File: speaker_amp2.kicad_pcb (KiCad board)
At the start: 2 copper layers, 72 parts, among them J1 Molex_430450227, J2 Molex_430450227, J3 Molex_430450227, J4 Molex_430450227, J5 Molex_1053101106, U1 TAS5822MDCPR, U2 TAS5822MDCPR

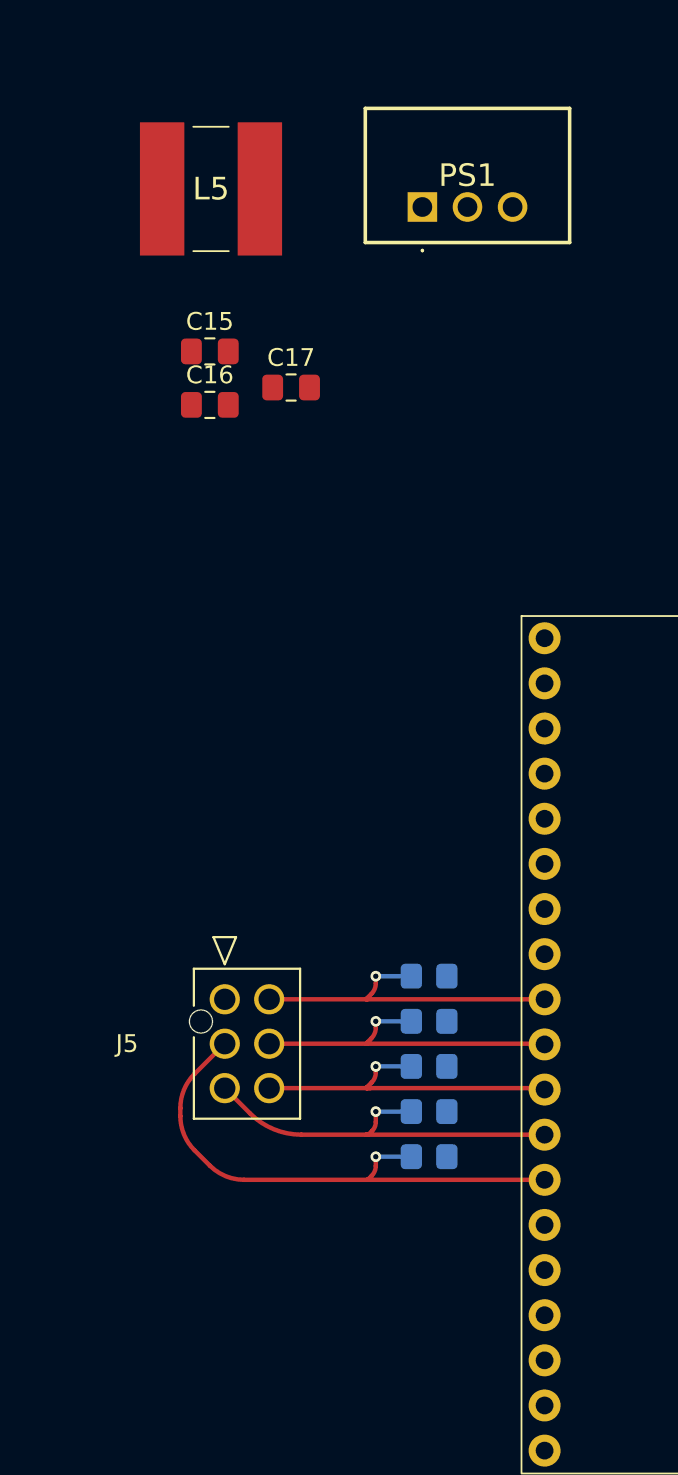
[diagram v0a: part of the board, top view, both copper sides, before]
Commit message: placed 3.3V to pcb
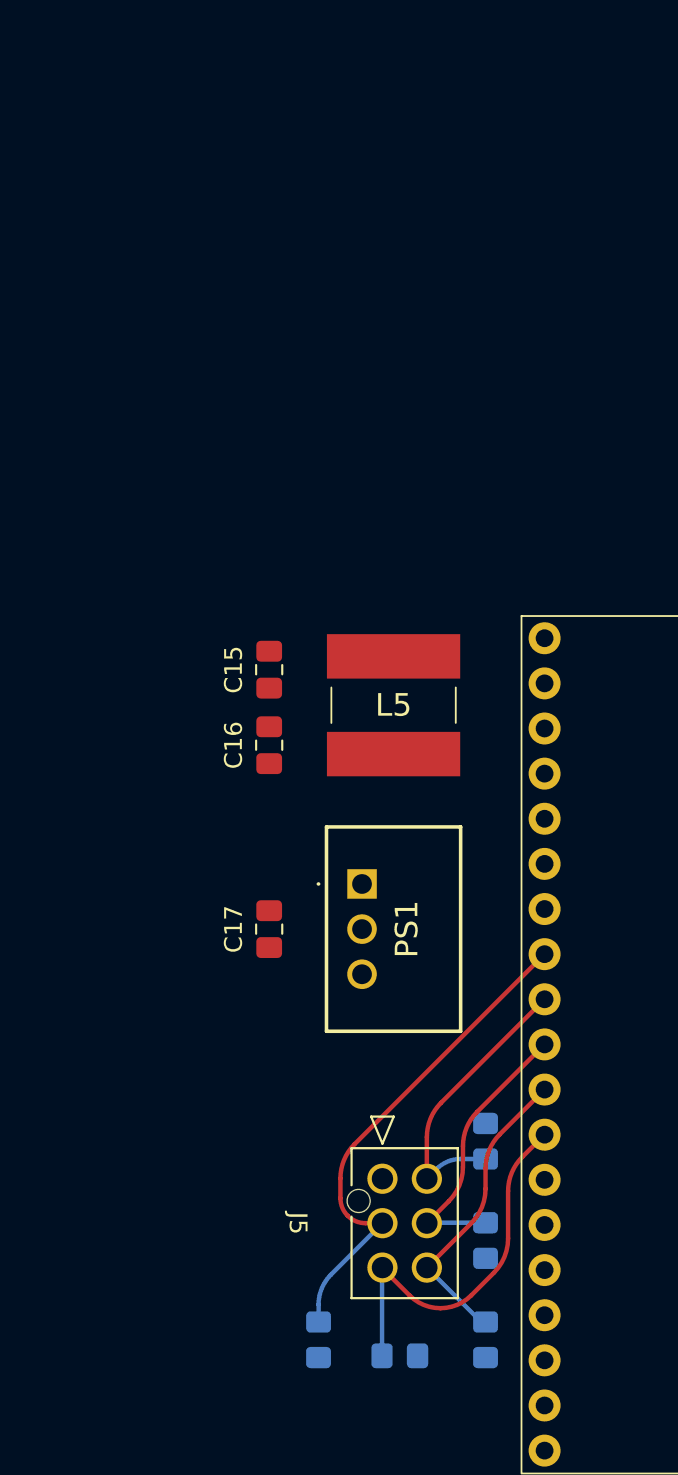
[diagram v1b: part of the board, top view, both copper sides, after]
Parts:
- moved PS1 38.3 mm to (36.0, 99.1), turned to -90 degrees
- moved L5 30.8 mm to (37.8, 89.0), turned to -90 degrees
- moved C17 30.5 mm to (30.8, 101.6), turned to 90 degrees
- moved C16 19.4 mm to (30.8, 91.2), turned to -90 degrees
- moved C15 18.2 mm to (30.8, 87.0), turned to 90 degrees
- moved R15 15.7 mm to (42.9, 124.7), turned to -90 degrees
- moved R12 13.8 mm to (38.1, 125.6)
- moved J5 13.4 mm to (37.1, 115.7)
- moved R14 12.7 mm to (42.9, 119.1), turned to -90 degrees
- moved R11 12.0 mm to (33.5, 124.7), turned to -90 degrees
- moved R13 9.82 mm to (42.9, 113.5), turned to 90 degrees
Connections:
- MCU1 pad 13: /Previous -> unconnected-(MCU1-GPIO12-Pad13)
- MCU1 pad 8: unconnected-(MCU1-GPIO33-Pad8) -> /Previous
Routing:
- net /Volume+: track 19.0 -> 15.9 mm, vias 1 -> 0
- net /Volume-: track 19.2 -> 16.4 mm, vias 1 -> 0
- net /Previous: track 30.8 -> 28.5 mm, vias 1 -> 0
- net /Play/Pause: track 19.1 -> 17.1 mm, vias 1 -> 0
- net /Next: track 22.5 -> 21.5 mm, vias 1 -> 0

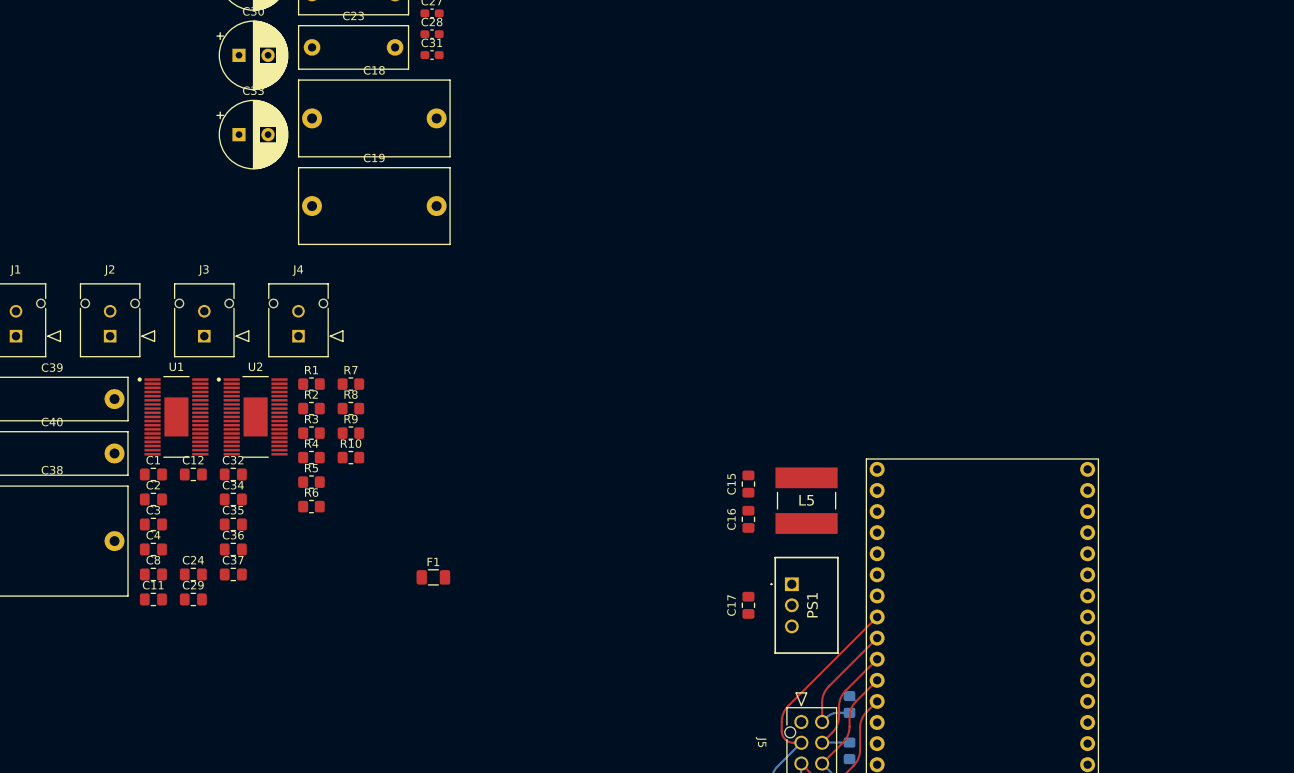
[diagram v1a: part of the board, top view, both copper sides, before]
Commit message: changed amplifiers in schematic to match PCB pins
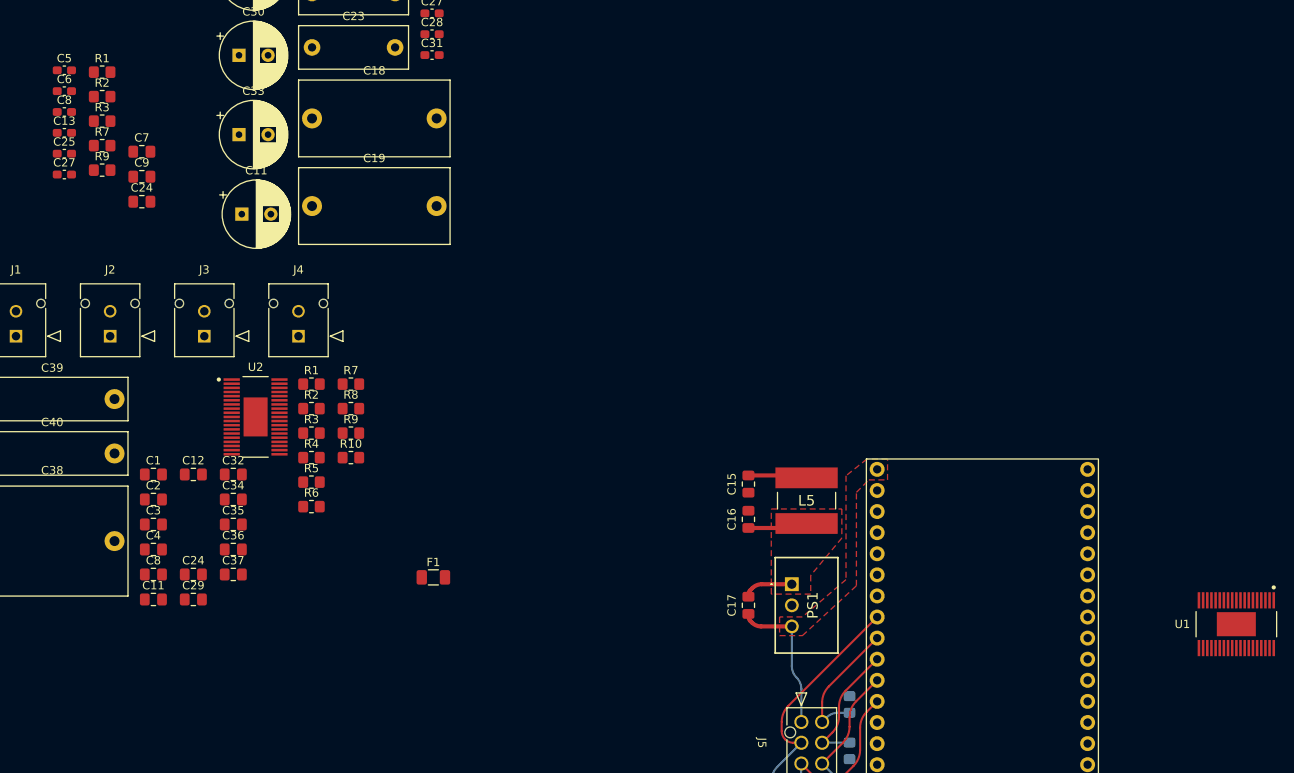
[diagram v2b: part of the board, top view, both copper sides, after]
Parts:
- added C11: 390u, Capacitor_THT:CP_Radial_D8.0mm_P3.50mm, F.Cu at (-30.2, 54.5)
- added C13: 1u, Capacitor_SMD:C_0603_1608Metric_Pad1.08x0.95mm_HandSolder, F.Cu at (-51.6, 44.7)
- added C24: 4.7u, Capacitor_SMD:C_0805_2012Metric_Pad1.18x1.45mm_HandSolder, F.Cu at (-42.3, 53.0)
- added C25: 0.1u, Capacitor_SMD:C_0603_1608Metric_Pad1.08x0.95mm_HandSolder, F.Cu at (-51.6, 47.2)
- added C27: 1u, Capacitor_SMD:C_0603_1608Metric_Pad1.08x0.95mm_HandSolder, F.Cu at (-51.6, 49.7)
- added C5: 0.1u, Capacitor_SMD:C_0603_1608Metric_Pad1.08x0.95mm_HandSolder, F.Cu at (-51.6, 37.2)
- added C6: 1u, Capacitor_SMD:C_0603_1608Metric_Pad1.08x0.95mm_HandSolder, F.Cu at (-51.6, 39.7)
- added C7: 4.7u, Capacitor_SMD:C_0805_2012Metric_Pad1.18x1.45mm_HandSolder, F.Cu at (-42.3, 47.0)
- added C8: 0.1u, Capacitor_SMD:C_0603_1608Metric_Pad1.08x0.95mm_HandSolder, F.Cu at (-51.6, 42.2)
- added C9: 22u, Capacitor_SMD:C_0805_2012Metric_Pad1.18x1.45mm_HandSolder, F.Cu at (-42.3, 50.0)
- added R1: 2.2k, Resistor_SMD:R_0805_2012Metric_Pad1.20x1.40mm_HandSolder, F.Cu at (-47.1, 37.4)
- added R2: 2.2k, Resistor_SMD:R_0805_2012Metric_Pad1.20x1.40mm_HandSolder, F.Cu at (-47.1, 40.4)
- added R3: 4.7k, Resistor_SMD:R_0805_2012Metric_Pad1.20x1.40mm_HandSolder, F.Cu at (-47.1, 43.3)
- added R7: 4.7k, Resistor_SMD:R_0805_2012Metric_Pad1.20x1.40mm_HandSolder, F.Cu at (-47.1, 46.2)
- added R9: 4.7k, Resistor_SMD:R_0805_2012Metric_Pad1.20x1.40mm_HandSolder, F.Cu at (-47.1, 49.2)
- moved U1 130.0 mm to (89.5, 103.9), turned to -90 degrees
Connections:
- net Net-(MCU1-GPIO17) renamed /PDN2
- net Net-(U1-SDOUT) renamed /SDOUT1
- C26 pad 1: Net-(U2-AVDD) -> GND
- C26 pad 2: GND -> Net-(U2-AVDD)
- C3 pad 1: Net-(U1-BST_B+) -> Net-(U1-BST_B-)
- C3 pad 2: Net-(U1-OUT_B+) -> Net-(U1-OUT_B-)
- C34 pad 1: Net-(U2-BST_A-) -> Net-(U2-OUT_A+)
- C34 pad 2: Net-(U2-OUT_A+) -> Net-(U2-BST_A-)
- C35 pad 1: Net-(U2-BST_A+) -> Net-(U2-OUT_A+)
- C35 pad 2: Net-(U2-OUT_A+) -> Net-(U2-BST_A+)
- C4 pad 1: Net-(U1-BST_B-) -> Net-(U1-BST_B+)
- C4 pad 2: Net-(U1-OUT_B-) -> Net-(U1-OUT_B+)
- L3 pad 1: Net-(U1-OUT_B+) -> Net-(U1-OUT_B-)
- L4 pad 2: Net-(U1-OUT_B-) -> Net-(U1-OUT_B+)
- L6 pad 1: Net-(U2-OUT_B+) -> Net-(U2-OUT_A+)
- L7 pad 2: Net-(U2-OUT_A+) -> Net-(U2-OUT_B+)
- MCU1 pad 21: Net-(MCU1-GPIO23) -> /ADR1
- MCU1 pad 22: Net-(MCU1-GPIO22) -> /LRCLK
- MCU1 pad 23: Net-(MCU1-GPIO1) -> /SCLK
- MCU1 pad 24: Net-(MCU1-GPIO3) -> /SDIN
- MCU1 pad 25: unconnected-(MCU1-GPIO21-Pad25) -> /SDA
- MCU1 pad 27: Net-(MCU1-GPIO19) -> /SCL
- MCU1 pad 28: Net-(MCU1-GPIO18) -> /PDN1
- MCU1 pad 29: Net-(MCU1-GPIO5) -> /ADR2
- MCU1 pad 31: Net-(MCU1-GPIO16) -> unconnected-(MCU1-GPIO16-Pad31)
- R4 pad 2: Net-(MCU1-GPIO5) -> /SDIN
- R6 pad 1: Net-(MCU1-GPIO16) -> /ADR2
- U1 pad 10: Net-(MCU1-GPIO1) -> /ADR1
- U1 pad 13: Net-(MCU1-GPIO19) -> /LRCLK
- U1 pad 14: Net-(MCU1-GPIO18) -> /SCLK
- U1 pad 15: Net-(MCU1-GPIO5) -> /SDIN
- U1 pad 27: Net-(MCU1-GPIO23) -> /SDA
- U1 pad 28: Net-(MCU1-GPIO22) -> /SCL
- U1 pad 29: Net-(MCU1-GPIO3) -> /PDN1
- U2 pad 10: Net-(MCU1-GPIO16) -> /ADR2
- U2 pad 13: Net-(MCU1-GPIO19) -> /LRCLK
- U2 pad 14: Net-(MCU1-GPIO18) -> /SCLK
- U2 pad 27: Net-(MCU1-GPIO23) -> /SDA
- U2 pad 28: Net-(MCU1-GPIO22) -> /SCL
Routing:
- net +3.3V: track 0.00 -> 17.9 mm
- net Net-(PS1-+VIN): track 0.00 -> 13.3 mm
- net PVDD: track 0.00 -> 7.12 mm
- added copper zone on F.Cu, net +3.3V
- added copper zone on F.Cu, net Net-(PS1-+VIN)

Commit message: placed amp ics, did low-voltage connections
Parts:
- removed the C27 at (-7.34, 30.3)
- U1, U2: footprint Speaker Amp Lib:DCP0038A-IPC_A -> Speaker Amp Lib:DCP0038A-IPC_B
- moved C11 190.2 mm to (141.2, 155.8)
- moved C13 190.2 mm to (151.5, 71.2)
- moved C2 190.2 mm to (141.2, 143.7)
- moved C25 190.2 mm to (130.5, 102.1)
- moved C29 190.2 mm to (146.0, 155.8)
- moved C3 190.2 mm to (141.2, 146.8)
- moved C30 190.2 mm to (151.5, 90.3)
- moved C33 190.2 mm to (151.5, 99.8)
- moved C34 190.2 mm to (150.8, 143.7)
- moved C35 190.2 mm to (150.8, 146.8)
- moved C37 190.2 mm to (150.8, 152.8)
- moved C5 190.2 mm to (130.5, 92.1)
- moved C8 190.2 mm to (141.2, 152.8)
- moved J1 190.2 mm to (124.6, 124.1)
- moved J2 190.2 mm to (136.0, 124.1)
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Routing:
- net PVDD: track 7.12 -> 67.3 mm, vias 0 -> 2
- net +3.3V: track 17.9 -> 60.3 mm, vias 0 -> 2
- net /SDA: track 0.00 -> 42.1 mm, vias 0 -> 2
- net /SCL: track 0.00 -> 36.4 mm, vias 0 -> 2
- net Net-(U2-SDIN): track 0.00 -> 12.6 mm
- net /SDOUT1: track 0.00 -> 6.19 mm
- net /PDN1: track 0.00 -> 5.77 mm, vias 0 -> 1
- net Net-(U2-VR_DIG): track 0.00 -> 3.81 mm
- net Net-(U2-AVDD): track 0.00 -> 3.34 mm
- net Net-(U1-AVDD): track 0.00 -> 3.12 mm
- net Net-(U1-VR_DIG): track 0.00 -> 2.96 mm
- net /SCLK: track 0.00 -> 2.67 mm, vias 0 -> 1
- net /ADR2: track 0.00 -> 2.17 mm, vias 0 -> 1
- net /LRCLK: track 0.00 -> 1.67 mm, vias 0 -> 1
- added copper zone on F.Cu, net Net-(F1-Pad2)

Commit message: changed some components (coils) for smaller ones
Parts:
- removed the C11 at (141.2, 155.8)
- removed the C13 at (82.5, 111.1)
- removed the C13 at (151.5, 71.2)
- removed the C24 at (84.2, 117.8)
- removed the C24 at (139.8, 107.9)
- removed the C25 at (84.0, 120.1)
- removed the C25 at (130.5, 102.1)
- removed the C5 at (174.7, 67.6)
- removed the C6 at (174.7, 70.2)
- removed the C7 at (174.7, 72.7)
- removed the C8 at (141.2, 152.8)
- removed the C8 at (84.5, 98.3)
- removed the C9 at (174.7, 75.2)
- removed the R1 at (160.2, 129.8)
- removed the R2 at (160.2, 132.8)
- removed the R3 at (160.2, 135.8)
- removed the R7 at (165.0, 129.8)
- removed the R9 at (165.0, 135.8)
- added C13: 1u, Capacitor_SMD:C_0603_1608Metric_Pad1.08x0.95mm_HandSolder, F.Cu at (79.2, 96.2)
- added C24: 4.7u, Capacitor_SMD:C_0805_2012Metric_Pad1.18x1.45mm_HandSolder, F.Cu at (77.8, 117.8)
- added C25: 0.1u, Capacitor_SMD:C_0603_1608Metric_Pad1.08x0.95mm_HandSolder, F.Cu at (80.0, 118.0)
- added C8: 0.1u, Capacitor_SMD:C_0603_1608Metric_Pad1.08x0.95mm_HandSolder, F.Cu at (79.8, 83.7)
- added F2: 2A, Fuse:Fuse_1206_3216Metric, F.Cu at (79.8, 138.5)
- added J6: Molex_430450227, Speaker Amp Lib:430450227_MOLEX, F.Cu at (65.3, 138.5)
- C11, C14, C27, C30, C33, C6: moved to B.Cu
- F1: value 8A -> 2A
- L1, L2, L3, L4: footprint Inductor_SMD:L_Wuerth_WE-PD-Typ-LS_Handsoldering -> Inductor_SMD:L_Wuerth_WE-PD-Typ-M-Typ-S_Handsoldering
- L6, L7: footprint Inductor_SMD:L_Wuerth_WE-PD-Typ-LS_Handsoldering -> Speaker Amp Lib:L_Wuerth_WE-PDF_Handsoldering_7mm_apart
- moved J1 130.1 mm to (254.0, 137.8)
- moved J2 130.1 mm to (265.3, 137.8)
- moved J3 130.1 mm to (276.7, 137.8)
- moved R10 112.8 mm to (53.8, 119.8)
- moved R8 112.8 mm to (53.8, 113.8)
- moved R6 108.6 mm to (53.5, 124.5)
- moved C31 100.5 mm to (83.2, 131.8), turned to 180 degrees
- moved C28 96.5 mm to (83.2, 118.5), turned to 180 degrees
- moved C10 93.5 mm to (83.4, 97.5)
- moved R1 80.4 mm to (54.8, 88.0)
- moved R2 80.4 mm to (54.8, 90.9)
- moved R3 80.4 mm to (54.8, 93.8)
- moved R7 80.4 mm to (54.8, 96.8)
- moved R9 80.4 mm to (54.8, 99.8)
- moved C33 76.9 mm to (84.0, 136.8)
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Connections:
- C28 pad 1: PVDD -> PVDD2
- C29 pad 1: PVDD -> PVDD2
- C30 pad 1: PVDD -> PVDD2
- C31 pad 1: PVDD -> PVDD2
- C32 pad 1: PVDD -> PVDD2
- C33 pad 1: PVDD -> PVDD2
- L2 pad 1: Net-(C18-Pad2) -> Net-(U1-OUT_A-)
- L2 pad 2: Net-(U1-OUT_A-) -> Net-(C18-Pad2)
- L4 pad 1: Net-(C19-Pad2) -> Net-(U1-OUT_B+)
- L4 pad 2: Net-(U1-OUT_B+) -> Net-(C19-Pad2)
- L7 pad 1: Net-(C38-Pad2) -> Net-(U2-OUT_B+)
- L7 pad 2: Net-(U2-OUT_B+) -> Net-(C38-Pad2)
- U2 pad 32: PVDD -> PVDD2
- U2 pad 33: PVDD -> PVDD2
- U2 pad 6: PVDD -> PVDD2
- U2 pad 7: PVDD -> PVDD2
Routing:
- net PVDD: track 67.3 -> 7.12 mm, vias 2 -> 0
- net +3.3V: track 60.3 -> 17.9 mm, vias 2 -> 0
- net /SDA: track 42.1 -> 0.00 mm, vias 2 -> 0
- net /SCL: track 36.4 -> 0.00 mm, vias 2 -> 0
- net Net-(U2-SDIN): track 12.6 -> 0.00 mm
- net /SDOUT1: track 6.19 -> 0.00 mm
- net /PDN1: track 5.77 -> 0.00 mm, vias 1 -> 0
- net Net-(U2-VR_DIG): track 3.81 -> 0.00 mm
- net Net-(U2-AVDD): track 3.34 -> 0.00 mm
- net Net-(U1-AVDD): track 3.12 -> 0.00 mm
- net Net-(U1-VR_DIG): track 2.96 -> 0.00 mm
- net /SCLK: track 2.67 -> 0.00 mm, vias 1 -> 0
- net /ADR2: track 2.17 -> 0.00 mm, vias 1 -> 0
- net /LRCLK: track 1.67 -> 0.00 mm, vias 1 -> 0
- removed copper zone on F.Cu, net Net-(F1-Pad2)

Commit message: changed output capacitors to smaller ones
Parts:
- C1, C2, C3, C34, C35, C36, C37, C4: footprint Capacitor_SMD:C_0805_2012Metric_Pad1.18x1.45mm_HandSolder -> Capacitor_SMD:C_0603_1608Metric_Pad1.08x0.95mm_HandSolder
- C17: moved to B.Cu
- C18, C19: footprint Capacitor_THT:C_Rect_L18.0mm_W9.0mm_P15.00mm_FKS3_FKP3 -> Speaker Amp Lib:C_2824
- C20, C21, C22, C23: footprint Capacitor_THT:C_Rect_L13.0mm_W5.0mm_P10.00mm_FKS3_FKP3_MKS4 -> Capacitor_SMD:C_2220_5750Metric_Pad1.97x5.40mm_HandSolder; moved to B.Cu
- C38: footprint Speaker Amp Lib:C_Rect_L18.0mm_W13.0mm_P15.00mm_FKS3_FKP3 -> Speaker Amp Lib:C_2824
- C39, C40: footprint Capacitor_THT:C_Rect_L18.0mm_W5.0mm_P15.00mm_FKS3_FKP3 -> Capacitor_SMD:C_2220_5750Metric_Pad1.97x5.40mm_HandSolder; moved to B.Cu
- moved J2 153.0 mm to (124.8, 77.5), turned to 180 degrees
- moved J3 149.3 mm to (127.8, 126.8), turned to 180 degrees
- moved J1 134.4 mm to (125.8, 97.5), turned to 180 degrees
- moved C1 129.3 mm to (88.5, 83.8), turned to 180 degrees
- moved C4 127.8 mm to (88.8, 95.5), turned to 180 degrees
- moved C2 126.7 mm to (91.8, 86.2), turned to 90 degrees
- moved C35 126.4 mm to (89.0, 122.5)
- moved C3 125.1 mm to (91.8, 92.8), turned to -90 degrees
- moved C37 124.9 mm to (89.4, 134.6), turned to 180 degrees
- moved C36 122.5 mm to (92.0, 130.3), turned to 90 degrees
- moved C34 122.1 mm to (92.0, 126.5), turned to 90 degrees
- moved C18 108.6 mm to (115.5, 79.2), turned to -90 degrees
- moved C22 106.3 mm to (116.0, 75.7)
- moved C19 106.3 mm to (116.2, 99.5), turned to -90 degrees
- moved C20 106.2 mm to (116.0, 83.0), turned to 180 degrees
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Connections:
- C34 pad 1: Net-(U2-OUT_A+) -> Net-(U2-BST_A-)
- C34 pad 2: Net-(U2-BST_A-) -> Net-(U2-OUT_A+)
- C35 pad 1: Net-(U2-OUT_A+) -> Net-(U2-BST_A+)
- C35 pad 2: Net-(U2-BST_A+) -> Net-(U2-OUT_A+)
- C36 pad 1: Net-(U2-BST_B-) -> Net-(U2-OUT_B+)
- C36 pad 2: Net-(U2-OUT_B+) -> Net-(U2-BST_B-)
- C37 pad 1: Net-(U2-BST_B+) -> Net-(U2-OUT_B+)
- C37 pad 2: Net-(U2-OUT_B+) -> Net-(U2-BST_B+)
- C39 pad 1: Net-(C38-Pad2) -> GND
- C39 pad 2: GND -> Net-(C38-Pad2)
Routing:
- net /Previous: track 28.5 -> 0.00 mm
- net /Next: track 21.5 -> 0.00 mm
- net +3.3V: track 17.9 -> 0.00 mm
- net /Play/Pause: track 17.1 -> 0.00 mm
- net /Volume-: track 16.4 -> 0.00 mm
- net /Volume+: track 15.9 -> 0.00 mm
- net Net-(PS1-+VIN): track 13.3 -> 0.00 mm
- net PVDD: track 7.12 -> 0.00 mm
- removed copper zone on F.Cu, net +3.3V
- removed copper zone on F.Cu, net Net-(PS1-+VIN)
